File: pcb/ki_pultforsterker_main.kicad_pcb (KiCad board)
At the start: 2 copper layers, 150 x 100 mm, 145 parts, among them J1 24V IN, J10 LED-RINGER, J2 SPK L, J3 SPK R, J4 AUX, J5 RPi 40-pin, J6 5V -> PI, J7 KNAPPER, J8 ENCODER, J9 OLED, K1 G6K-2P-Y 5VDC, Q1 AO3400A, Q2 AO3400A, Q3 AO3400A, Q4 AO3400A, Q5 AO3400A, Q6 AO3400A, U1 TPS54560BDDA, U2 AMS1117-3.3, U3 ICL7660, U4 PCM5102APW, U5 PGA2311UA, U6 TPA3116D2DAD

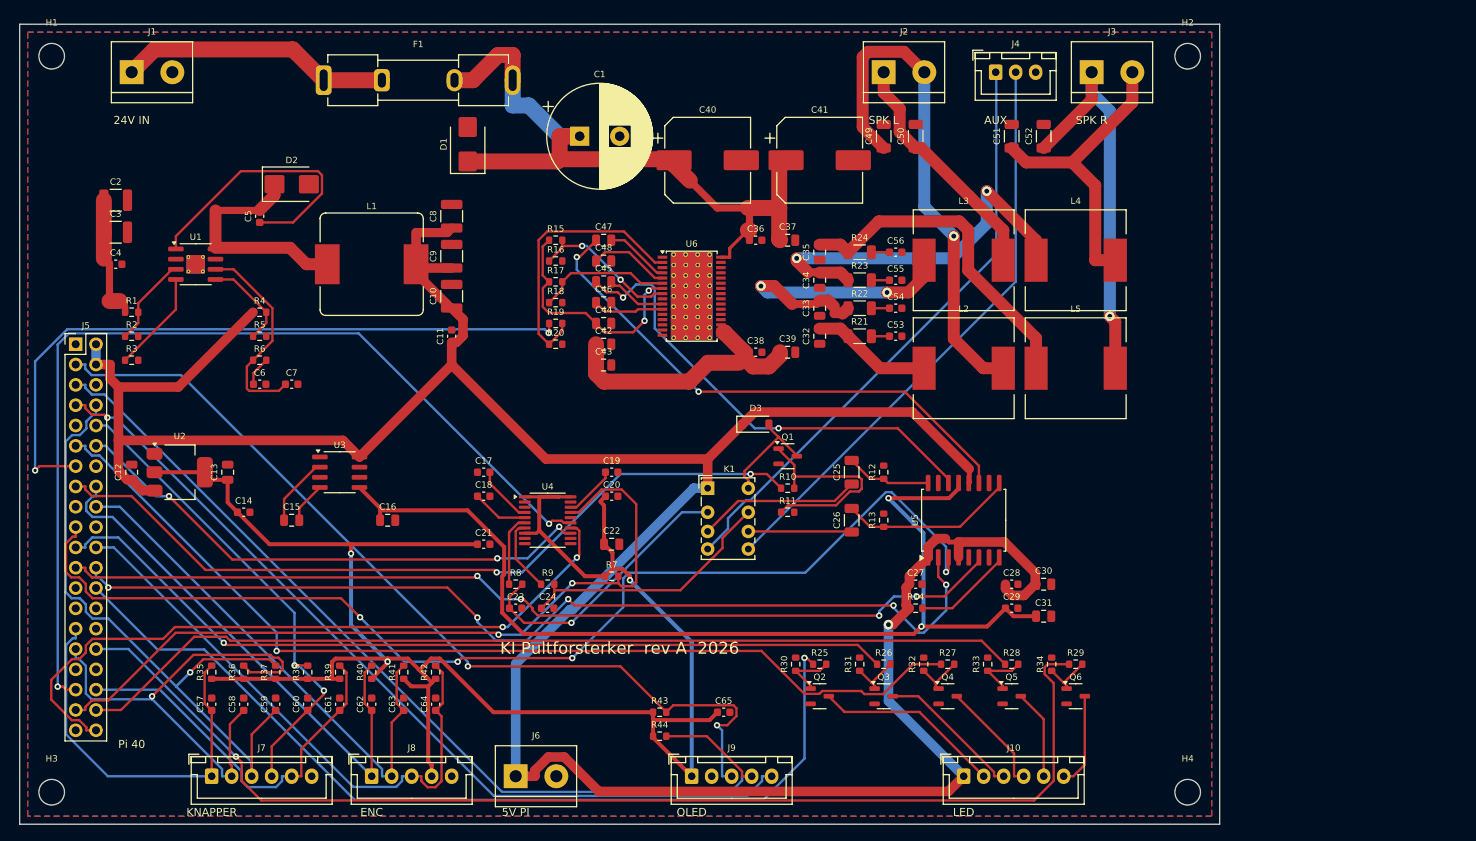
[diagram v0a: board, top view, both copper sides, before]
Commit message: PCB: eksport med SES-parser, sporutvidelse og DRC via pcbnew
Co-Authored-By: Claude Fable 5.1 <noreply@anthropic.com>
Claude-Session: https://claude.ai/code/session_01FaJKmYinw8SWRobKXBRYpt
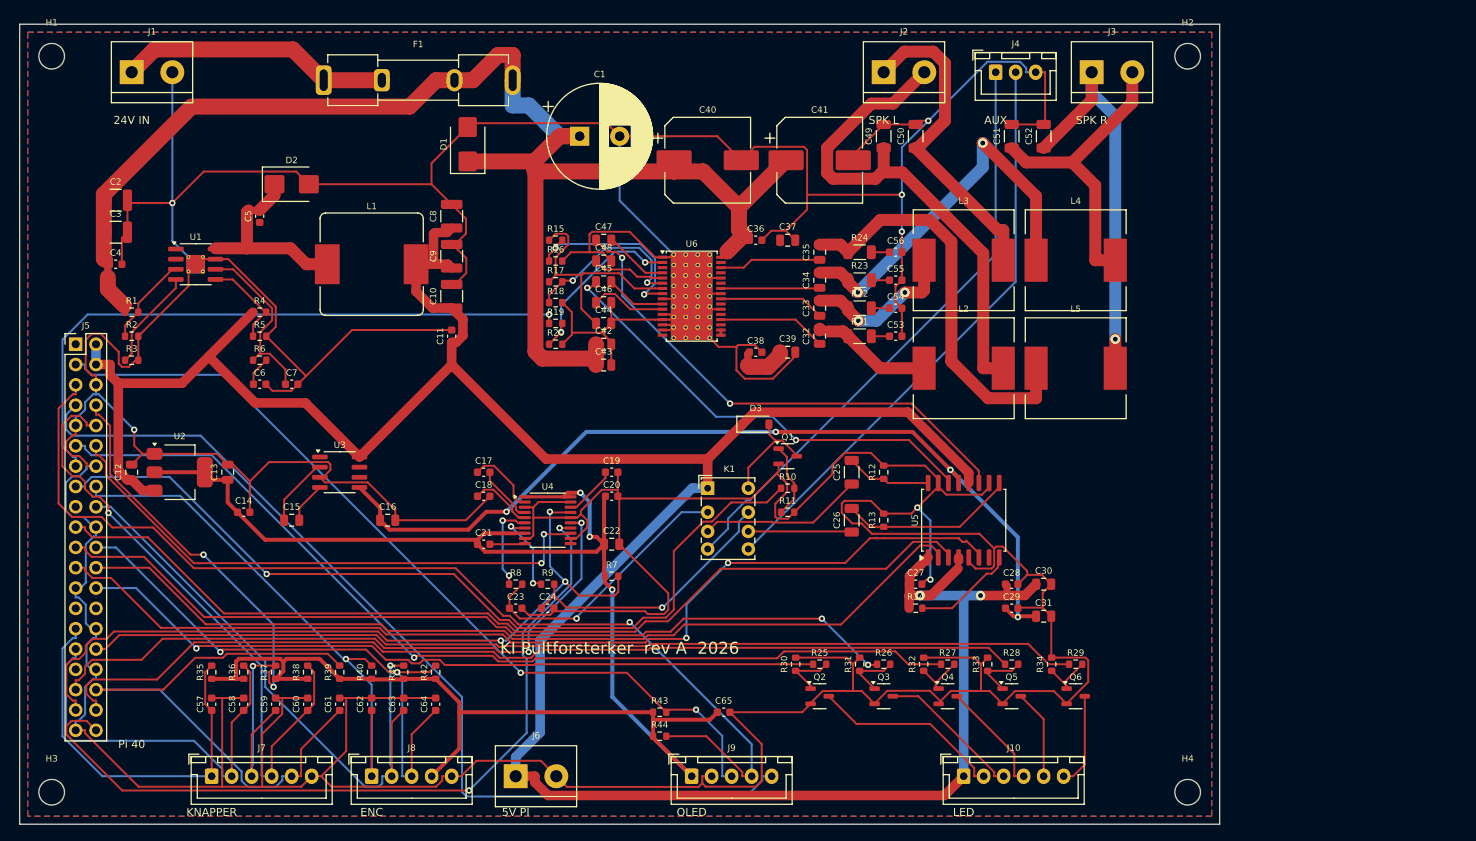
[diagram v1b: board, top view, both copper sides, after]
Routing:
- net GND: track 0.00 -> 1059.3 mm, vias 0 -> 7
- net VIN24: track 143.9 -> 194.3 mm
- net I2S_LRCK: track 120.0 -> 81.4 mm
- net BUCK_BOOT: track 35.0 -> 0.00 mm
- net BTN_PWR: track 48.8 -> 75.4 mm
- net LED_PWR_G: track 147.8 -> 124.2 mm, vias 1 -> 0
- net LED_AIR_G: track 115.7 -> 94.3 mm
- net SPI_MOSI: track 140.4 -> 120.5 mm, vias 4 -> 0
- net OUTPL: track 37.1 -> 19.6 mm
- net RLY_GATE: track 26.8 -> 9.45 mm
- net BTN_USB: track 61.1 -> 78.2 mm, vias 2 -> 1
- net VNEG: track 128.4 -> 112.3 mm, vias 2 -> 4
- net BTN_BT: track 63.9 -> 49.9 mm, vias 1 -> 0
- net 5V: track 367.4 -> 353.6 mm, vias 1 -> 2
- net BSNL: track 0.00 -> 13.6 mm
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
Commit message: PCB: SES importeres som s-expr, bootstrap-kondensatorer flyttet, klaring 0,15 mm
Co-Authored-By: Claude Fable 5.1 <noreply@anthropic.com>
Claude-Session: https://claude.ai/code/session_01FaJKmYinw8SWRobKXBRYpt
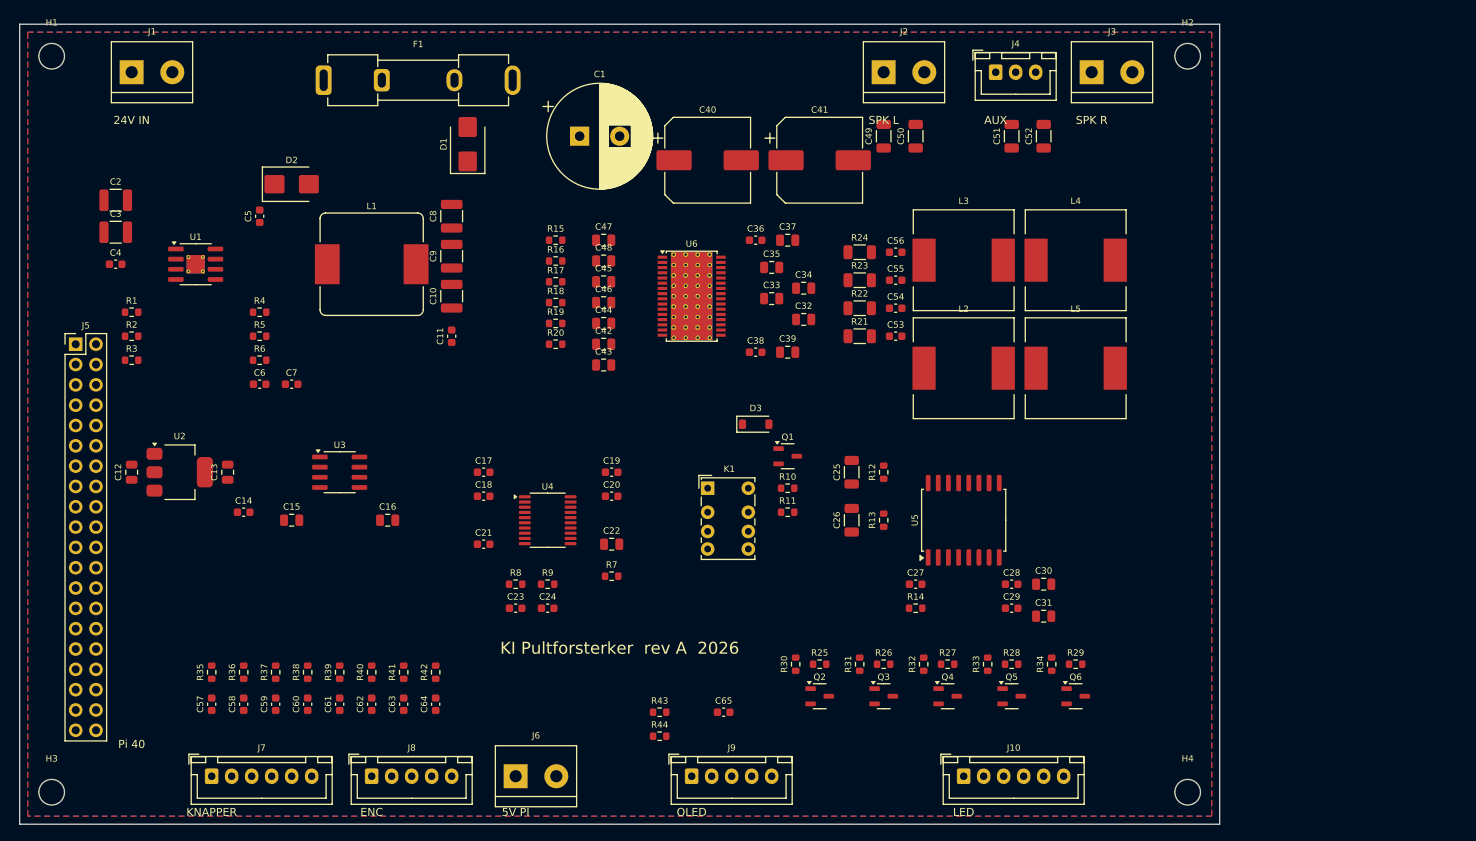
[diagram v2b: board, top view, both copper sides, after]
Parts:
- moved C35 6.29 mm to (94.0, 30.4), turned to 0 degrees
- moved C33 6.12 mm to (94.0, 34.3), turned to 0 degrees
- moved C32 2.90 mm to (98.0, 36.9), turned to 0 degrees
- moved C34 2.24 mm to (98.0, 33.0), turned to 0 degrees
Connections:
- U1 pad : (no net) -> GND
- U6 pad : (no net) -> GND
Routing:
- net GND: track 1059.3 -> 0.00 mm, vias 7 -> 0
- net 5V: track 353.6 -> 0.00 mm, vias 2 -> 0
- net 3V3: track 221.4 -> 0.00 mm, vias 3 -> 0
- net VIN24: track 194.3 -> 0.00 mm
- net SCL: track 132.3 -> 0.00 mm, vias 1 -> 0
- net SPI_SCLK: track 126.3 -> 0.00 mm, vias 2 -> 0
- net LED_PWR_G: track 124.2 -> 0.00 mm
- net LED_USB_G: track 123.0 -> 0.00 mm
- net LED_AUX_G: track 120.9 -> 0.00 mm, vias 1 -> 0
- net SPI_MOSI: track 120.5 -> 0.00 mm
- net OLED_RES: track 119.0 -> 0.00 mm
- net SPI_CS: track 114.8 -> 0.00 mm
- net VNEG: track 112.3 -> 0.00 mm, vias 4 -> 0
- net RLY_G: track 108.2 -> 0.00 mm, vias 1 -> 0
- net LED_BT_G: track 108.2 -> 0.00 mm, vias 2 -> 0
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
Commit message: PCB: faste forruter i DSN, DRC-styrt sporbredde
Co-Authored-By: Claude Fable 5.1 <noreply@anthropic.com>
Claude-Session: https://claude.ai/code/session_01FaJKmYinw8SWRobKXBRYpt
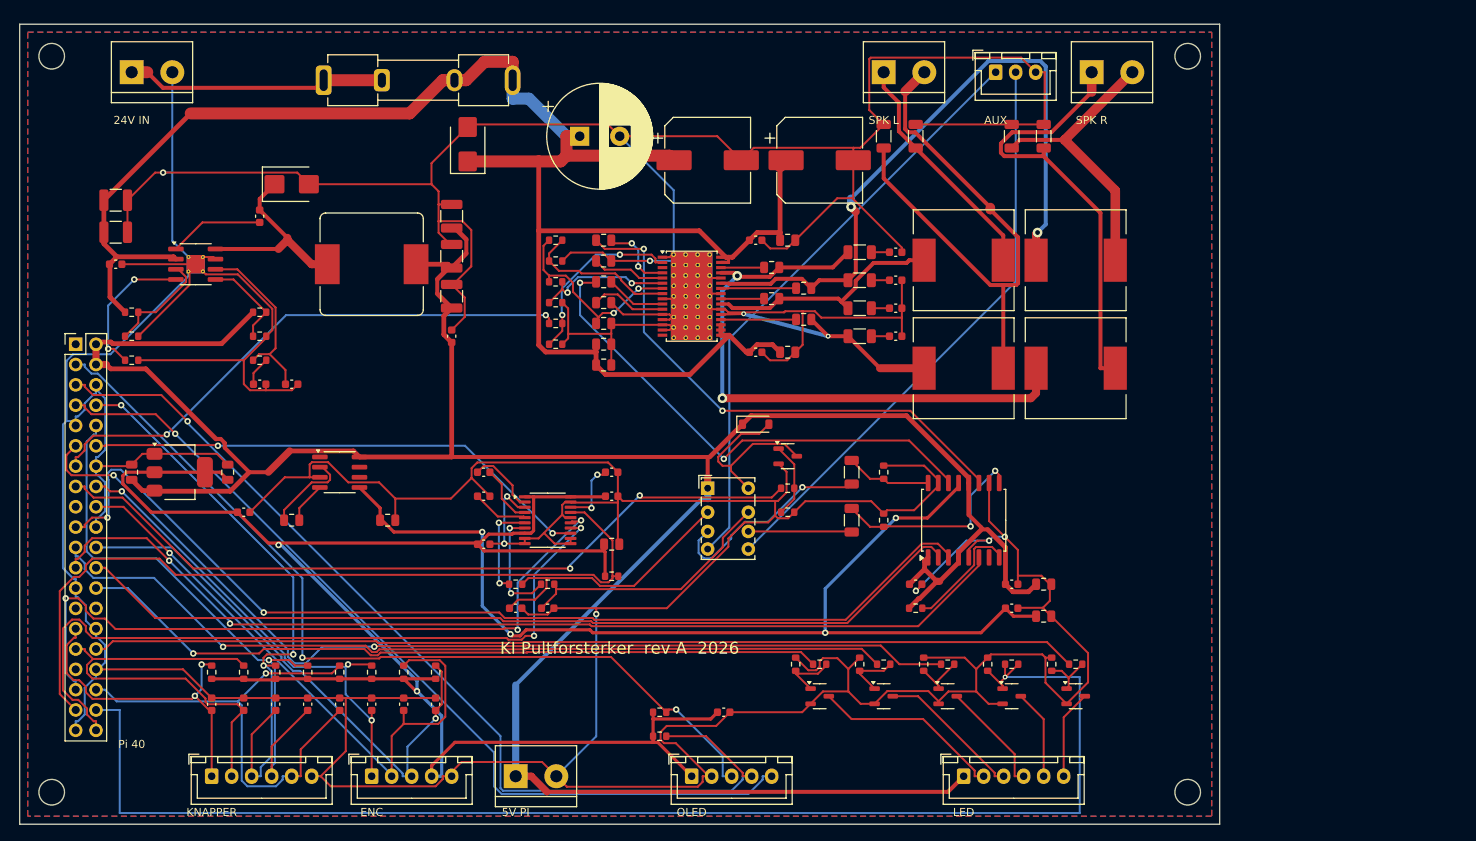
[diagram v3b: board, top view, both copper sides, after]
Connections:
- U1 pad : GND -> (no net)
- U6 pad : GND -> (no net)
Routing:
- net GND: track 0.00 -> 1090.8 mm, vias 0 -> 8
- net 5V: track 0.00 -> 348.1 mm
- net VIN24: track 0.00 -> 234.9 mm
- net 3V3: track 0.00 -> 222.8 mm, vias 0 -> 2
- net LED_USB_G: track 0.00 -> 163.8 mm, vias 0 -> 1
- net VNEG: track 0.00 -> 128.9 mm, vias 0 -> 4
- net SPI_MOSI: track 0.00 -> 128.2 mm, vias 0 -> 2
- net LED_AUX_G: track 0.00 -> 125.3 mm, vias 0 -> 2
- net SPI_SCLK: track 0.00 -> 124.4 mm, vias 0 -> 2
- net SCL: track 0.00 -> 123.6 mm, vias 0 -> 1
- net LED_PWR_G: track 0.00 -> 123.3 mm
- net SPI_CS: track 0.00 -> 112.9 mm
- net SDA: track 0.00 -> 111.2 mm, vias 0 -> 2
- net OLED_RES: track 0.00 -> 110.9 mm, vias 0 -> 1
- net LED_BT_G: track 0.00 -> 107.8 mm, vias 0 -> 1
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
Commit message: PCB: faste forruter i riktig enhet (µm)
Co-Authored-By: Claude Fable 5.1 <noreply@anthropic.com>
Claude-Session: https://claude.ai/code/session_01FaJKmYinw8SWRobKXBRYpt
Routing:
- net GND: track 1090.8 -> 0.00 mm, vias 8 -> 0
- net 5V: track 348.1 -> 0.00 mm
- net VIN24: track 234.9 -> 0.00 mm
- net 3V3: track 222.8 -> 0.00 mm, vias 2 -> 0
- net LED_USB_G: track 163.8 -> 0.00 mm, vias 1 -> 0
- net VNEG: track 128.9 -> 0.00 mm, vias 4 -> 0
- net SPI_MOSI: track 128.2 -> 0.00 mm, vias 2 -> 0
- net LED_AUX_G: track 125.3 -> 0.00 mm, vias 2 -> 0
- net SPI_SCLK: track 124.4 -> 0.00 mm, vias 2 -> 0
- net SCL: track 123.6 -> 0.00 mm, vias 1 -> 0
- net LED_PWR_G: track 123.3 -> 0.00 mm
- net SPI_CS: track 112.9 -> 0.00 mm
- net SDA: track 111.2 -> 0.00 mm, vias 2 -> 0
- net OLED_RES: track 110.9 -> 0.00 mm, vias 1 -> 0
- net LED_BT_G: track 107.8 -> 0.00 mm, vias 1 -> 0
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
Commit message: PCB: OUTPR forrutet fast
Co-Authored-By: Claude Fable 5.1 <noreply@anthropic.com>
Claude-Session: https://claude.ai/code/session_01FaJKmYinw8SWRobKXBRYpt
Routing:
- net GND: track 0.00 -> 1117.5 mm, vias 0 -> 9
- net 5V: track 0.00 -> 350.7 mm, vias 0 -> 3
- net 3V3: track 0.00 -> 238.8 mm, vias 0 -> 1
- net VIN24: track 0.00 -> 221.9 mm, vias 0 -> 1
- net LED_USB_G: track 0.00 -> 163.8 mm, vias 0 -> 1
- net SCL: track 0.00 -> 145.1 mm, vias 0 -> 1
- net OLED_RES: track 0.00 -> 130.5 mm, vias 0 -> 1
- net SDA: track 0.00 -> 127.6 mm, vias 0 -> 1
- net LED_AUX_G: track 0.00 -> 126.3 mm, vias 0 -> 1
- net SPI_SCLK: track 0.00 -> 123.5 mm, vias 0 -> 2
- net LED_PWR_G: track 0.00 -> 122.9 mm
- net SPI_MOSI: track 0.00 -> 119.1 mm
- net VNEG: track 0.00 -> 116.6 mm, vias 0 -> 4
- net SPI_CS: track 0.00 -> 113.3 mm
- net LED_BT_G: track 0.00 -> 106.9 mm, vias 0 -> 2
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
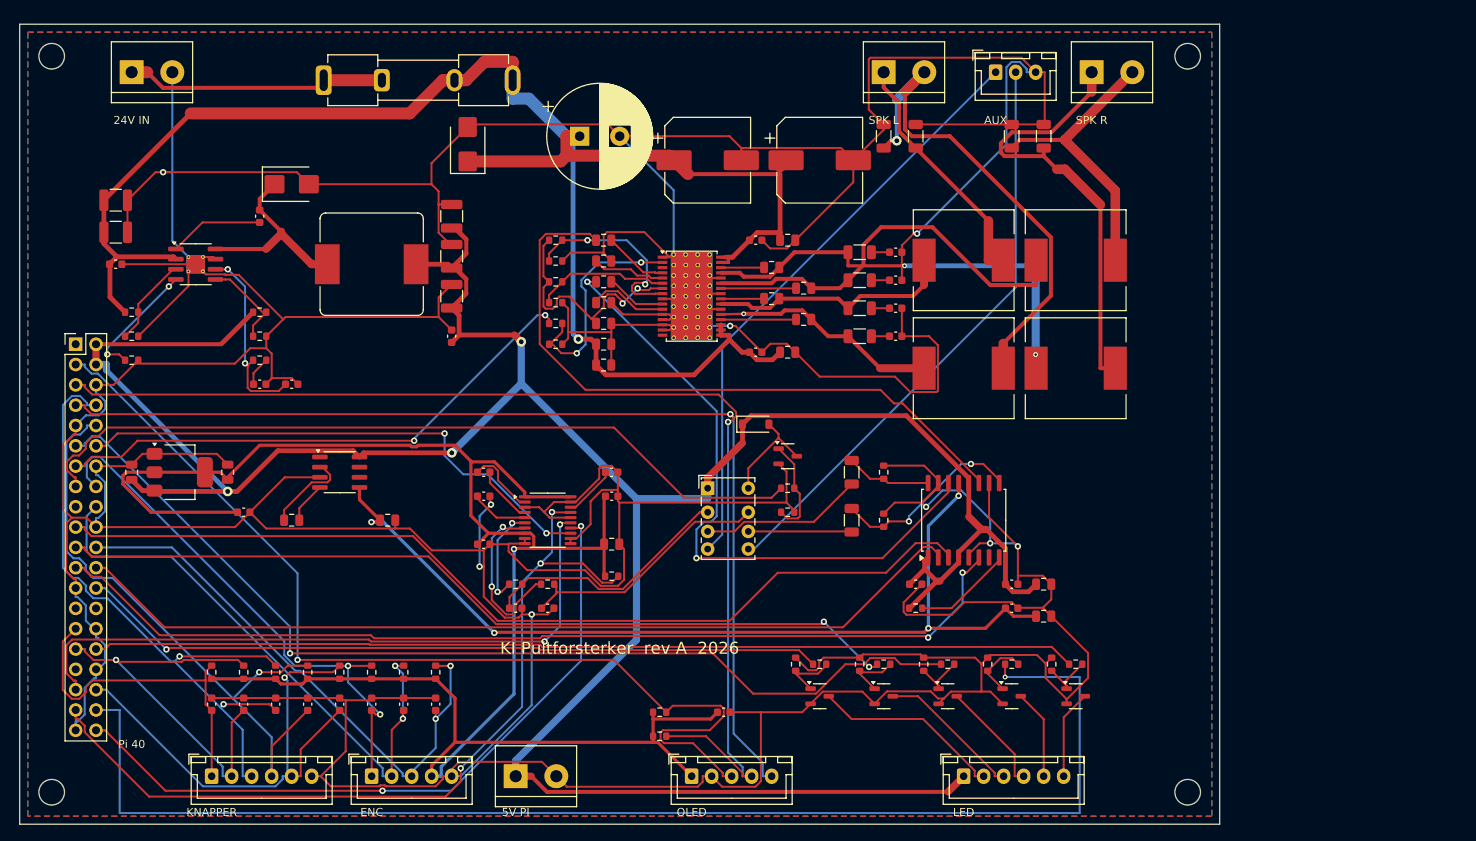
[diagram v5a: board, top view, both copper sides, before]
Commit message: Hovedkort rev A: ferdig rutet, DRC uten koblings-/klaringsfeil, produksjonsfiler (Gerber, BOM, CPL inkl. THT)
Co-Authored-By: Claude Fable 5.1 <noreply@anthropic.com>
Claude-Session: https://claude.ai/code/session_01FaJKmYinw8SWRobKXBRYpt
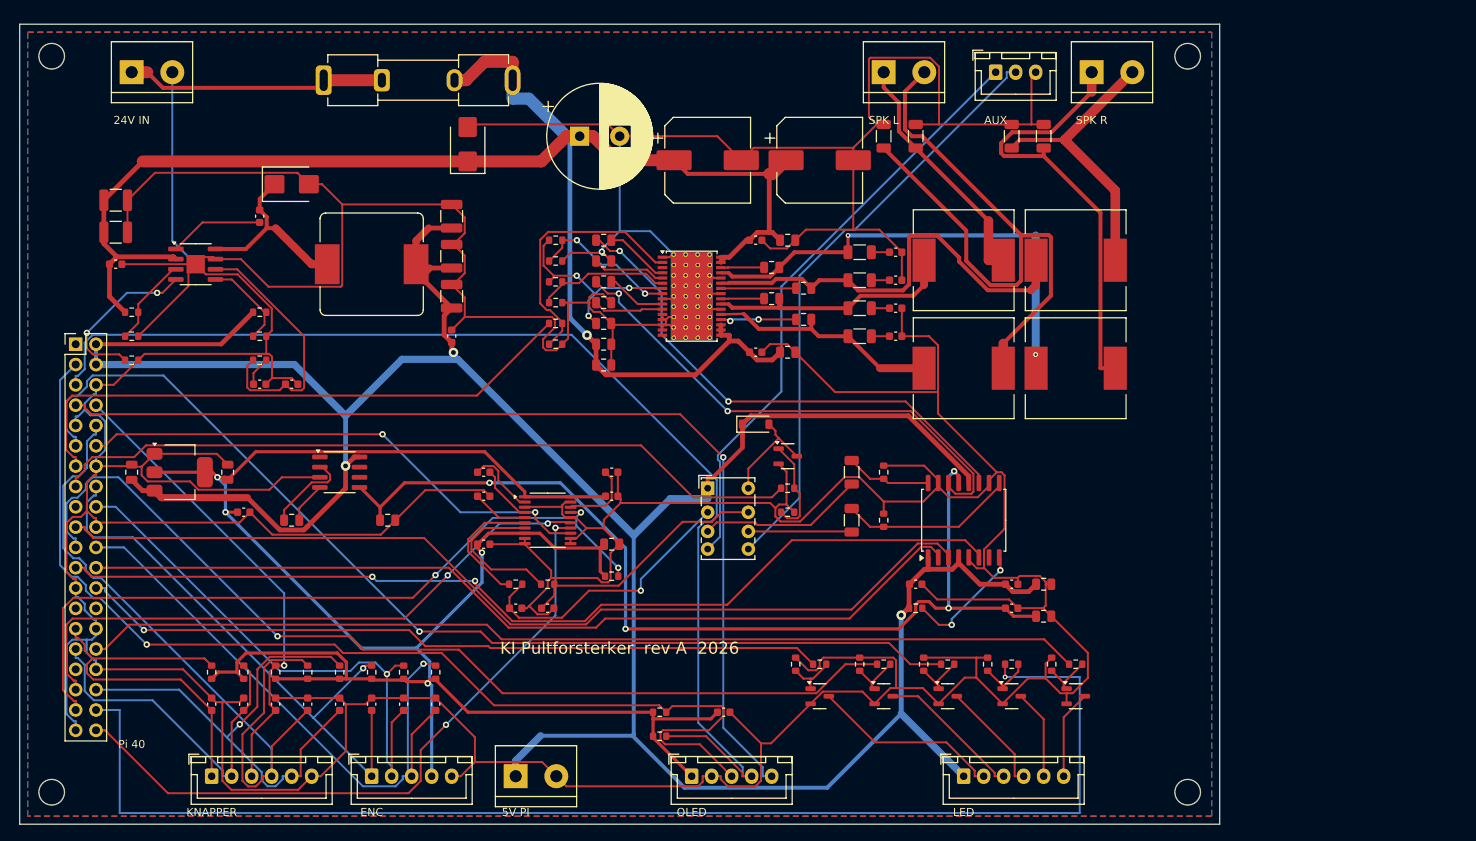
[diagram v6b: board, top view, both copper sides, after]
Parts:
- U1: footprint HSOP-8-1EP_3.9x4.9mm_P1.27mm_EP2.3x2.3mm_ThermalVias -> HSOP-8-1EP_3.9x4.9mm_P1.27mm_EP2.3x2.3mm
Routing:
- net GND: track 1117.5 -> 1091.3 mm, vias 9 -> 1
- net BTN_AUX: track 84.6 -> 59.1 mm, vias 2 -> 1
- net SPK_LN: track 62.8 -> 83.2 mm, vias 1 -> 0
- net VOL_OUTR: track 83.0 -> 64.1 mm, vias 0 -> 2
- net VOL_OUTL: track 80.0 -> 64.0 mm
- net LED_BT_G: track 106.9 -> 121.9 mm, vias 2 -> 1
- net BTN_USB: track 80.1 -> 94.1 mm, vias 1 -> 0
- net DAC_XSMT: track 106.3 -> 94.0 mm
- net 5V: track 350.7 -> 361.8 mm
- net SDA: track 127.6 -> 138.6 mm
- net BUCK_COMP: track 23.6 -> 32.7 mm, vias 2 -> 0
- net ENC_SW: track 70.5 -> 78.5 mm, vias 2 -> 1
- net BTN_BT: track 52.2 -> 44.2 mm, vias 1 -> 0
- net VNEG: track 116.6 -> 123.8 mm
- net VIN24: track 221.9 -> 214.8 mm
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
